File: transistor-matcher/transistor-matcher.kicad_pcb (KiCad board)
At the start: 2 copper layers, 39.4 x 82.6 mm, 14 parts, among them J1 V+, J2 GND, J3 V-, J4 DMM1, J5 Conn_01x05_Female, J6 Conn_01x05_Female, J7 DMM2, SW1 SW_DPDT_x2

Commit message: Updating ordered boards
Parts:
- moved J2 7.46 mm to (108.8, 42.5)
- moved H1 6.39 mm to (112.5, 107.2)
- moved J3 3.49 mm to (98.8, 42.5)
- moved J4 1.73 mm to (90.0, 116.3)
- moved J7 0.97 mm to (100.0, 116.2)
- moved J1 0.49 mm to (88.8, 42.5)
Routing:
- net Net-(J3-Pad1): track 47.1 -> 34.9 mm
- net Net-(J4-Pad1): track 51.7 -> 51.0 mm
- net Net-(J6-Pad2): track 45.7 -> 45.1 mm
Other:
- board size 39.4 x 82.6 mm -> 40 x 83.5 mm
- board text added: "+V"
- board text added: "-V"
- board text added: "DMM+"
- board text added: "DMM-"
- board text added: "GND"

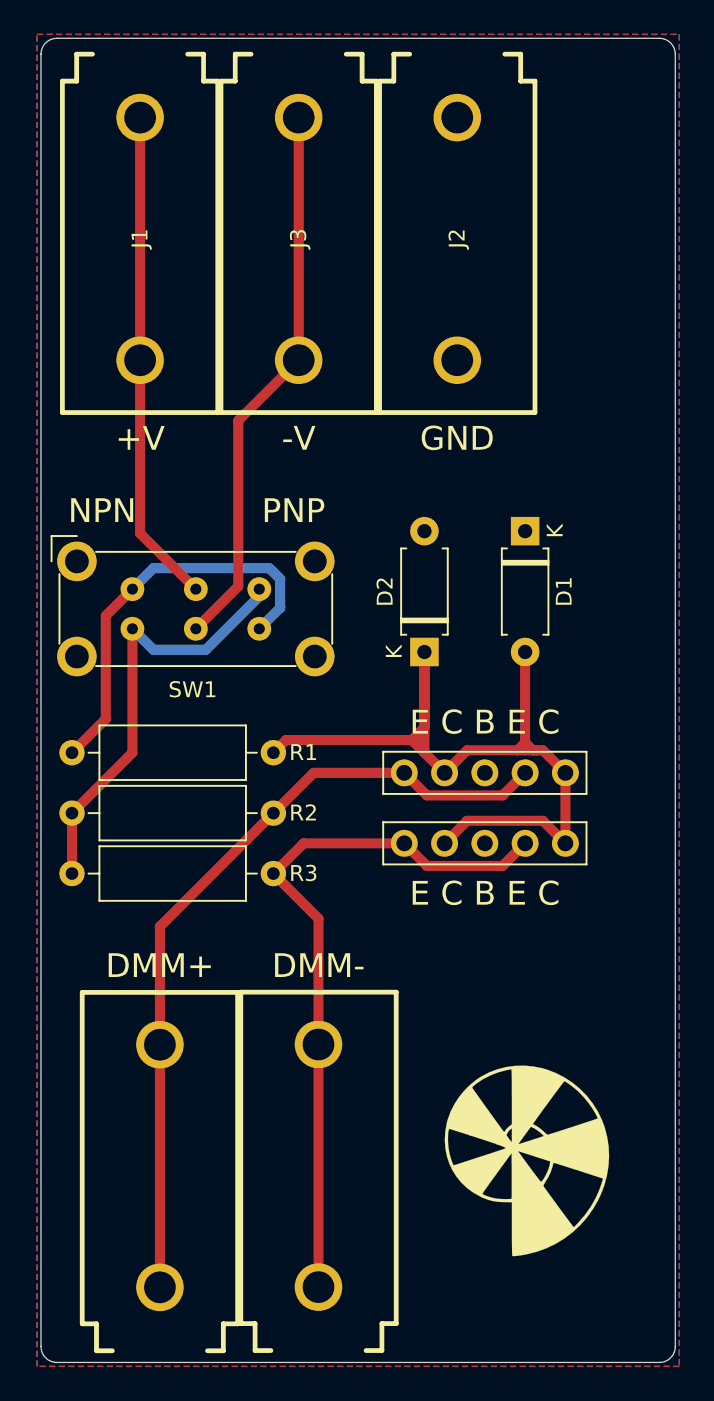
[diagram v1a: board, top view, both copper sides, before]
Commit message: Tweak transistor matcher and generate gerbers
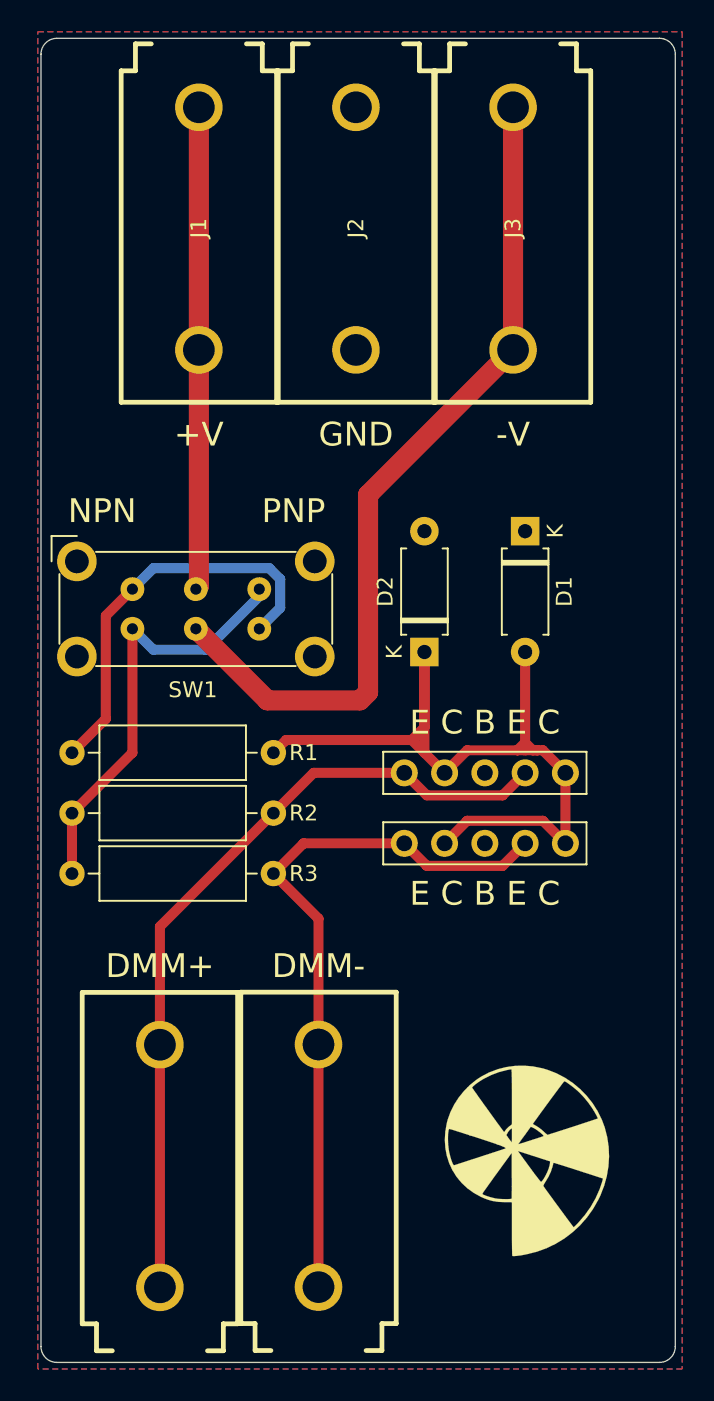
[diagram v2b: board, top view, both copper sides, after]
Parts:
- moved J3 13.5 mm to (112.3, 41.9)
- moved J2 6.42 mm to (102.4, 41.9)
- moved J1 3.76 mm to (92.5, 41.9)
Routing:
- net Net-(J3-Pad1): track 34.9 -> 53.6 mm
- net Net-(J1-Pad1): track 31.2 -> 30.5 mm
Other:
- rule pad_to_mask_clearance: 0.0508 -> 0
